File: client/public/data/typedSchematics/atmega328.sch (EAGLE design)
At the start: 7 parts, among them U3 ATMEGA328, Y1 8MHz

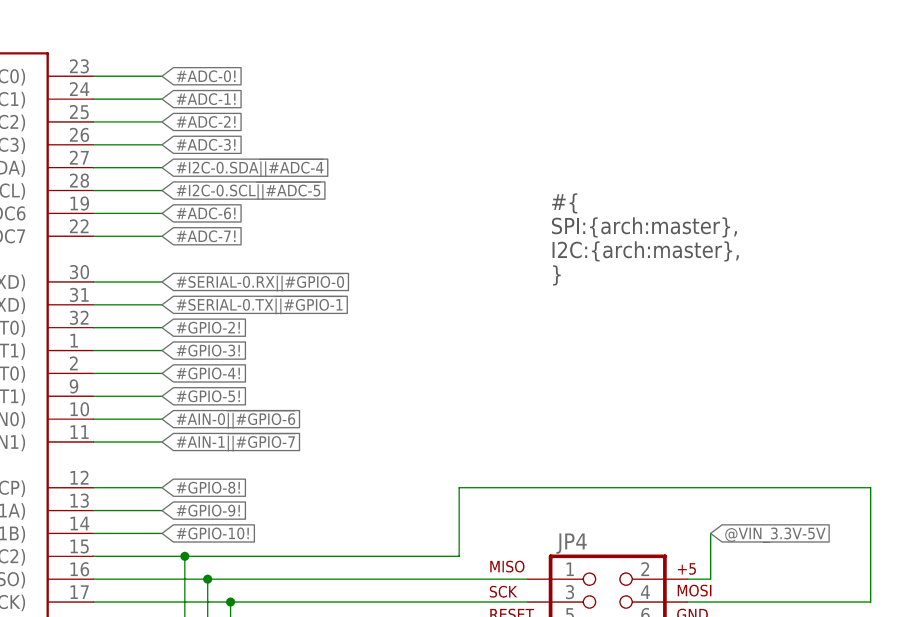
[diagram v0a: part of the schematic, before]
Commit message: Configuring schematics with blocktype info
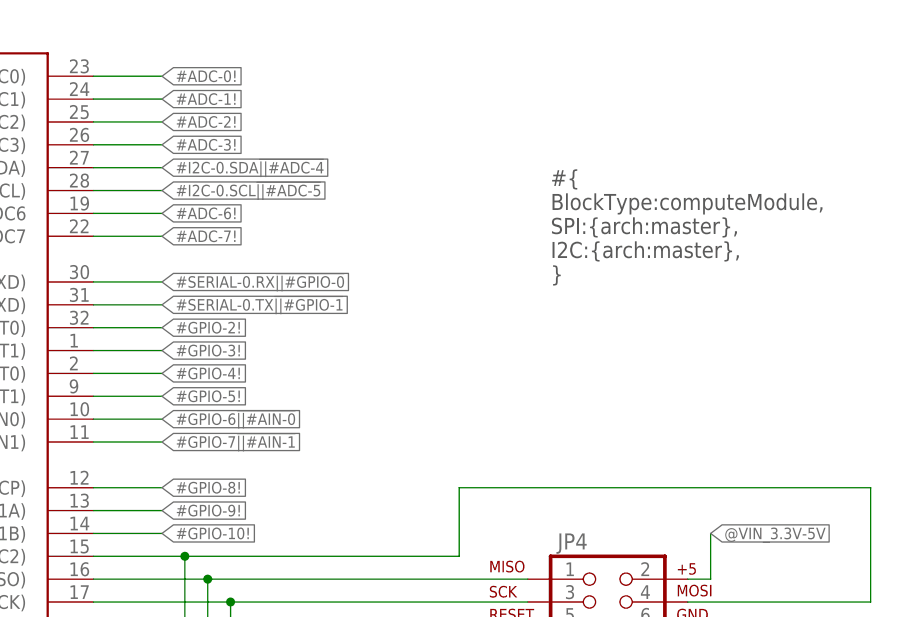
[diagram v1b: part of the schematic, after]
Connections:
- net #AIN-0!||#GPIO-6! renamed #GPIO-6!||#AIN-0!
- net #AIN-1!||#GPIO-7! renamed #GPIO-7!||#AIN-1!
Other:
- note added: "#{ BlockType:computeModule, SPI:{arch:master}, I2C:{arch:master}, }"
- note removed: "#{ SPI:{arch:master}, I2C:{arch:master}, }"
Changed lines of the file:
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@@
 <plain>
 <text x="175.26" y="101.6" size="1.778" layer="97">#{
+BlockType:computeModule,
 SPI:{arch:master},
 I2C:{arch:master},
@@
 </segment>
 </net>
-<net name="#AIN-0!||#GPIO-6!" class="0">
+<net name="#GPIO-6!||#AIN-0!" class="0">
 <segment>
 <pinref part="U3" gate="G$1" pin="PD6(AIN0)"/>
@@
 </segment>
 </net>
-<net name="#AIN-1!||#GPIO-7!" class="0">
+<net name="#GPIO-7!||#AIN-1!" class="0">
 <segment>
 <pinref part="U3" gate="G$1" pin="PD7(AIN1)"/>

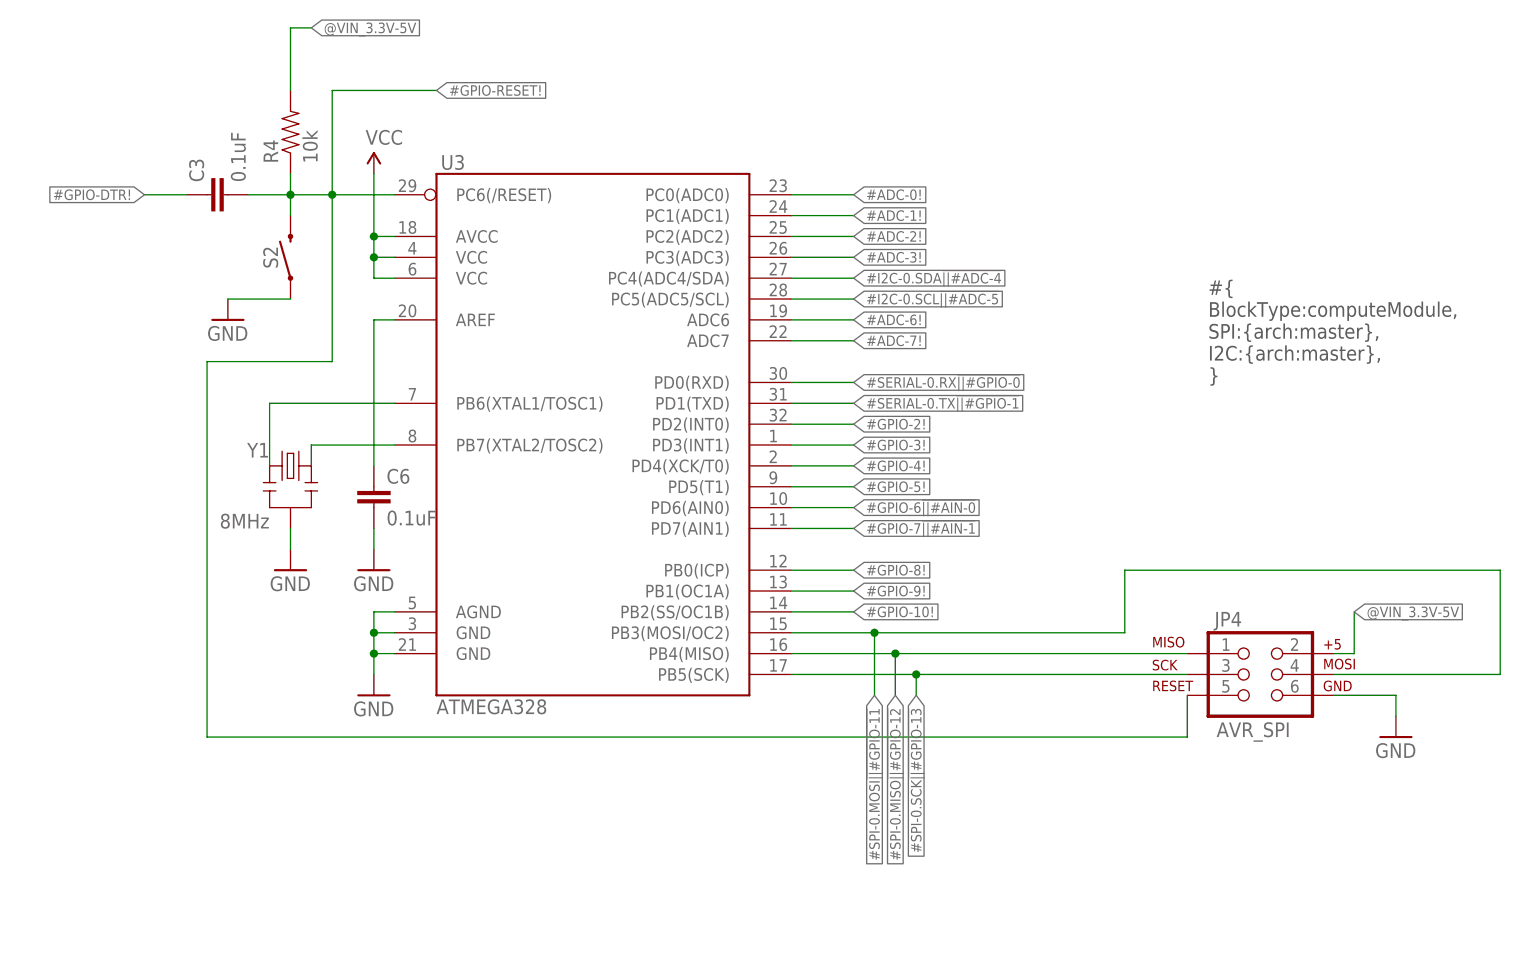
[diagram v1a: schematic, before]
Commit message: Adding Mat Tsch to UI
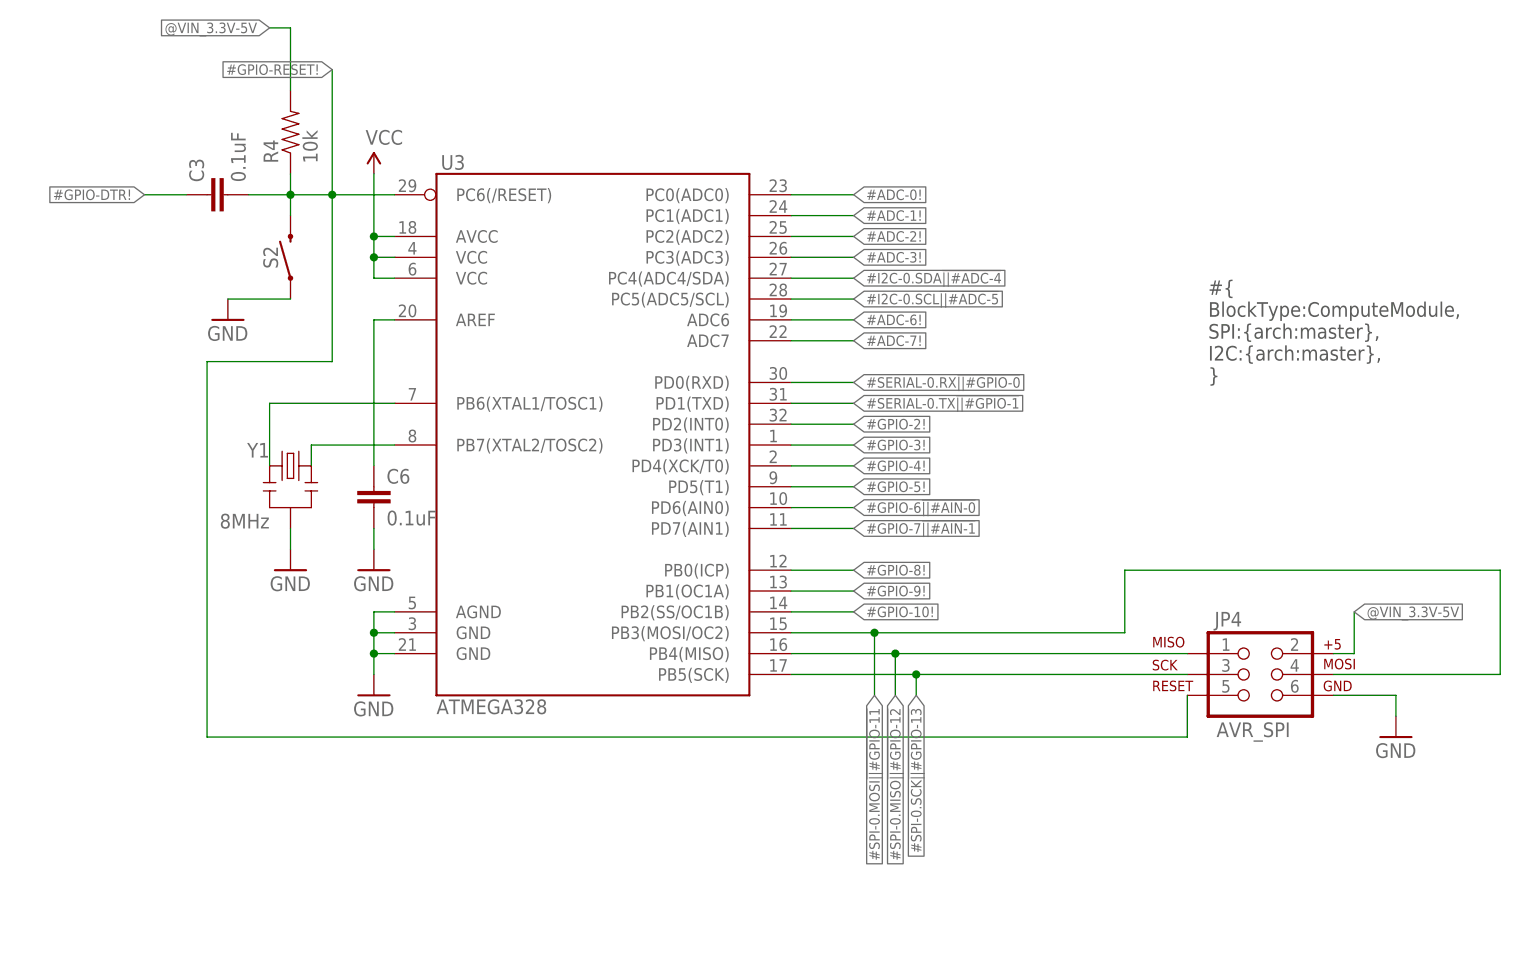
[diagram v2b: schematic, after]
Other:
- note added: "#{ BlockType:ComputeModule, SPI:{arch:master}, I2C:{arch:master}, }"
- note removed: "#{ BlockType:computeModule, SPI:{arch:master}, I2C:{arch:master}, }"
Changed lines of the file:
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@@
 <plain>
 <text x="175.26" y="101.6" size="1.778" layer="97">#{
-BlockType:computeModule,
+BlockType:ComputeModule,
 SPI:{arch:master},
 I2C:{arch:master},
@@
 <pinref part="S2" gate="G$1" pin="2"/>
 <junction x="68.58" y="124.46"/>
-<wire x1="68.58" y1="124.46" x2="68.58" y2="137.16" width="0.1524" layer="91"/>
-<wire x1="68.58" y1="137.16" x2="81.28" y2="137.16" width="0.1524" layer="91"/>
-<label x="81.28" y="137.16" size="1.27" layer="95" xref="yes"/>
+<wire x1="68.58" y1="124.46" x2="68.58" y2="139.7" width="0.1524" layer="91"/>
+<label x="68.58" y="139.7" size="1.27" layer="95" rot="R180" xref="yes"/>
 <pinref part="JP4" gate="G$1" pin="5"/>
 <wire x1="172.72" y1="63.5" x2="172.72" y2="58.42" width="0.1524" layer="91"/>
@@
 <pinref part="R4" gate="G$1" pin="2"/>
 <wire x1="63.5" y1="137.16" x2="63.5" y2="144.78" width="0.1524" layer="91"/>
-<wire x1="63.5" y1="144.78" x2="66.04" y2="144.78" width="0.1524" layer="91"/>
-<label x="66.04" y="144.78" size="1.27" layer="95" xref="yes"/>
-</segment>
-<segment>
+<wire x1="63.5" y1="144.78" x2="60.96" y2="144.78" width="0.1524" layer="91"/>
+<label x="60.96" y="144.78" size="1.27" layer="95" rot="R180" xref="yes"/>
+</segment>
+<segment>
